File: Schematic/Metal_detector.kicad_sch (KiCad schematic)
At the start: 56 parts, among them J1 3.5mm jack, Q1 BC550, U1 NUCLEO64-F411RE, U2 LM393, U3 PCA9635

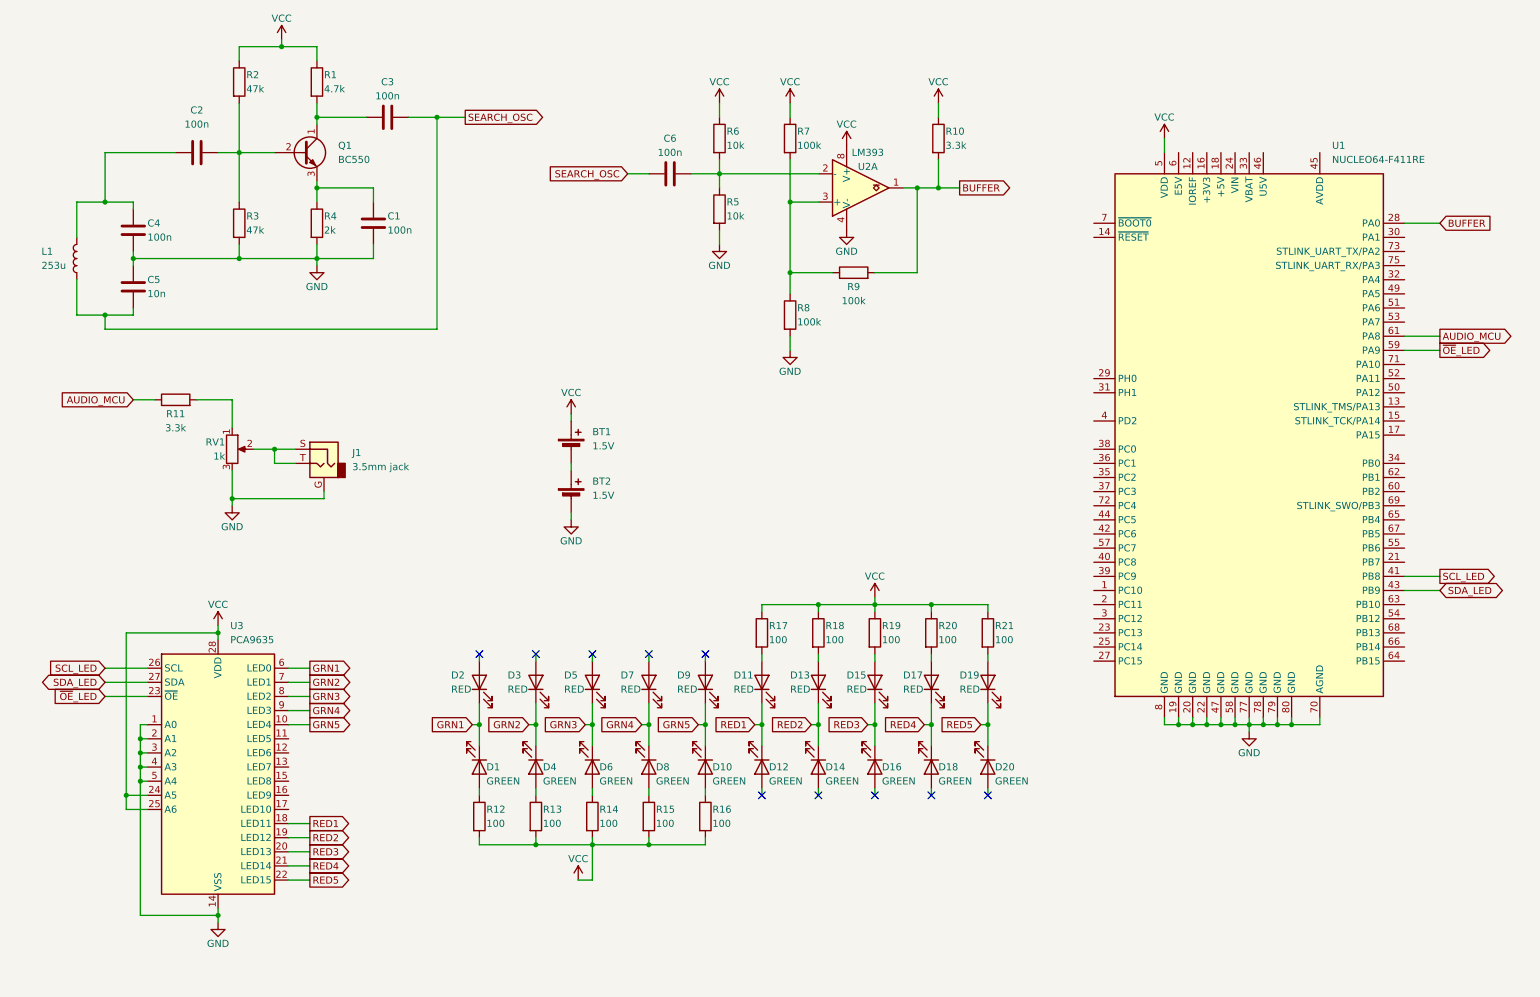
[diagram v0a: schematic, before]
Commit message: Added block diagram and schematic
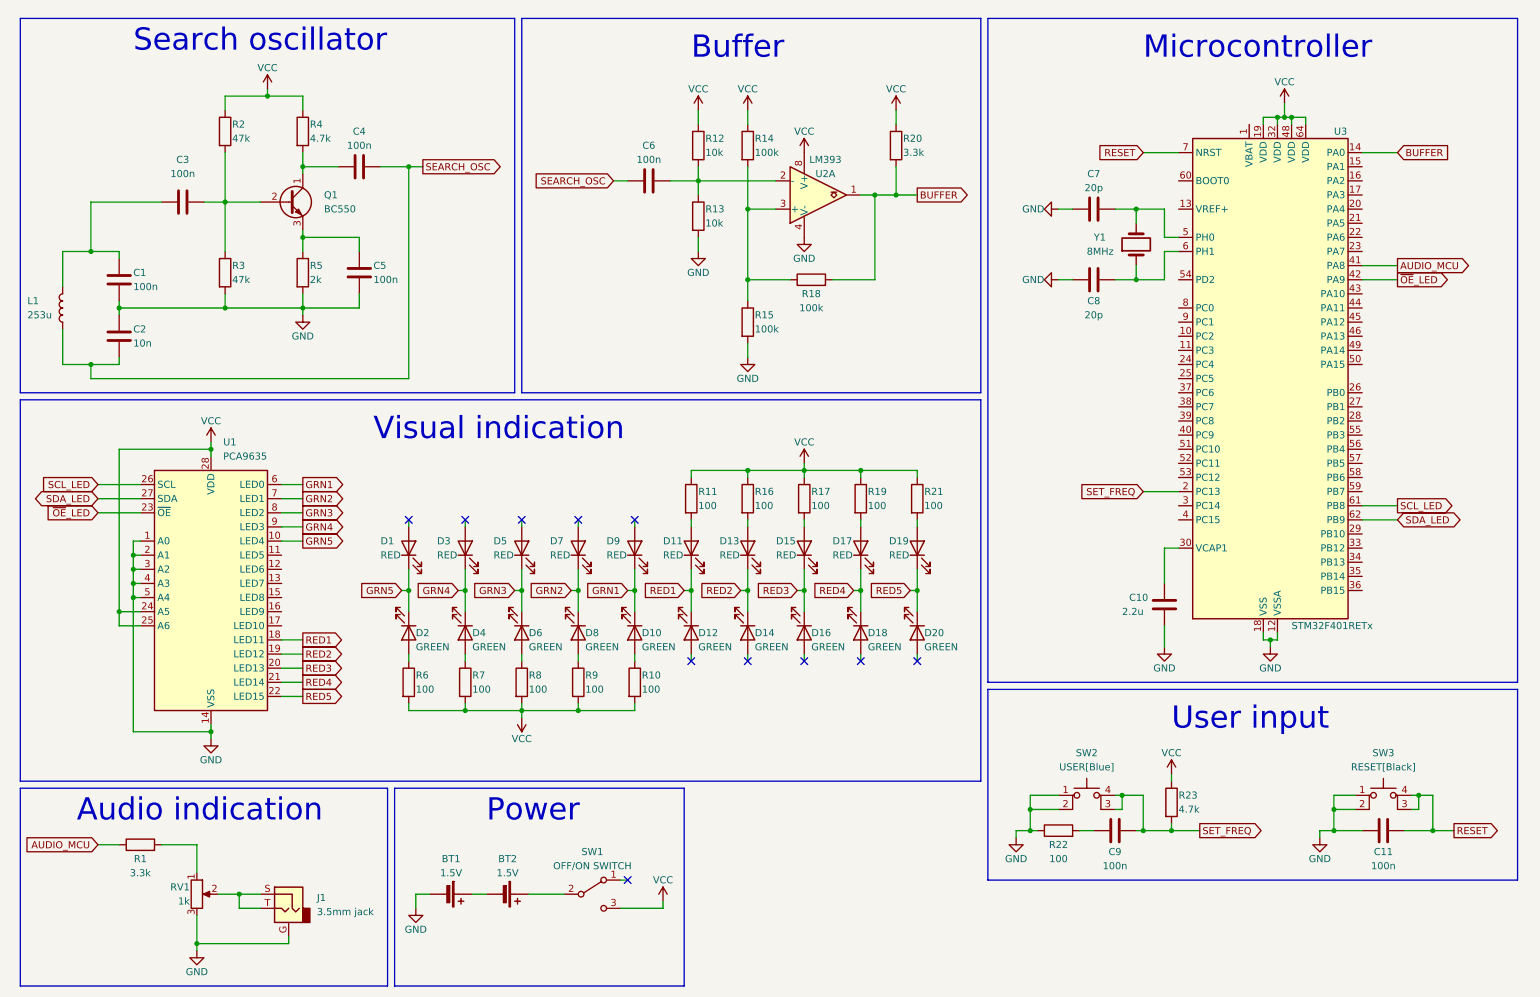
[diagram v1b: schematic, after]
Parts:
- removed U1: NUCLEO64-F411RE, Module:ST_Morpho_Connector_144_STLink, symbol MCU_Module:NUCLEO64-F411RE
- added C10: 2.2u, symbol Device:C
- added C11, C9: 100n, symbol Device:C
- added C7, C8: 20p, symbol Device:C
- added R22: 100, symbol Device:R
- added R23: 4.7k, symbol Device:R
- added SW1: OFF/ON SWITCH, symbol Switch:SW_SPDT
- added SW2: USER[Blue], symbol Switch:SW_MEC_5E
- added SW3: RESET[Black], symbol Switch:SW_MEC_5E
- added U3: STM32F401RETx, Package_QFP:LQFP-64_10x10mm_P0.5mm, symbol MCU_ST_STM32F4:STM32F401RETx
- added Y1: 8MHz, symbol Device:Crystal
- renumbered C4 to C1, C5 to C2, C2 to C3, C3 to C4, C1 to C5, D2 to D1, D1 to D2, R11 to R1, R16 to R10, R17 to R11, R6 to R12, R5 to R13, R7 to R14, R8 to R15, R18 to R16, R19 to R17, R9 to R18, R20 to R19, R10 to R20, R1 to R4, R4 to R5, R12 to R6, R13 to R7, R14 to R8, R15 to R9, U3 to U1
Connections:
- net AUDIO_MCU: now also U3.41 (PA8)
- net BUFFER: now also U3.14 (PA0)
- net GND: now also BT1.2 (-), C10.2, C11.1, C7.1, C8.1, R22.1, SW2.1, SW2.2, SW3.1, SW3.2, U3.12 (VSSA), U3.18 (VSS), U3.31 (VSS), U3.47 (VSS), U3.63 (VSS); no longer BT2.2 (-)
- net GRN1: now also D10.1 (K), D9.1 (K); no longer D1.1 (K), D2.1 (K)
- net GRN2: now also D7.1 (K), D8.1 (K); no longer D3.1 (K), D4.1 (K)
- net GRN4: now also D3.1 (K), D4.1 (K); no longer D7.1 (K), D8.1 (K)
- net GRN5: now also D1.1 (K), D2.1 (K); no longer D10.1 (K), D9.1 (K)
- net SCL_LED: now also U3.61 (PB8)
- net SDA_LED: now also U3.62 (PB9)
- net VCC: now also R23.1, SW1.3 (C), U3.19 (VDD), U3.32 (VDD), U3.48 (VDD), U3.64 (VDD); no longer BT1.1 (+)
- net ~{OE}_LED: now also U3.42 (PA9)
- net at BT2.1 (+): now also SW1.2 (B); no longer BT1.2 (-)
- new net: C10.1, U3.30 (VCAP1)
- new net: C9.1, R22.2
- new net: C7.2, U3.5 (PH0), Y1.2
- new net: C8.2, U3.6 (PH1), Y1.1
- new net: BT1.1 (+), BT2.2 (-)
- new net RESET: C11.2, SW3.3 (K), SW3.4 (A), U3.7 (NRST)
- new net SET_FREQ: C9.2, R23.2, SW2.3 (K), SW2.4 (A), U3.2 (PC13)
- no-connect marks 10 -> 11
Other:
- note added: "Audio indication"
- note added: "Buffer"
- note added: "Microcontroller"
- note added: "Power"
- note added: "Search oscillator"
- note added: "User input"
- note added: "Visual indication"
- company: (none) -> TU-Sofia
- title: (none) -> Metal detector
- moved on the sheet: C1, C2, C3, C4, C5, C6, D1, D10, D11, D12, D13, D14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

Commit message: Edited the oscillator block and wrote documentation for it
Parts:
- added C12: 47u, symbol Device:C_Polarized
- added C13, C14, C15, C16: 100n, symbol Device:C
- added R24: 1, symbol Device:R
- L1: value 253u -> 281u
- R14, R15: value 100k -> 10k
- R2: value 47k -> 20k
- R3: value 47k -> 10k
- R4: value 4.7k -> 1.2k
- R5: value 2k -> 330
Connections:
- net GND: now also C12.2, C13.2, C14.2, C15.2, C16.2
- net VCC: now also C13.1, C14.1, C15.1, C16.1, R24.1
- new net: C12.1, R24.2
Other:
- note added: "IC filter caps"
- note added: "Osc filter"

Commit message: Edited and documented the search oscillator, buffer and mcu blocks
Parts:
- removed C14: 100n, symbol Device:C
- added R24: 10k, symbol Device:R
- C14: renamed from C10; value 2.2u -> 4.7u
- C5: value 100n -> 1u
- renumbered C16 to C10, C7 to C11, C8 to C12, C9 to C13, C11 to C15, C12 to C7, C13 to C8, C15 to C9, R24 to R12, R12 to R13, R13 to R14, R14 to R15, R15 to R16, R16 to R17, R17 to R18, R18 to R19, R19 to R20, R20 to R21, R21 to R22, R22 to R23, R23 to R25
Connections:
- net GND: now also R24.1
- net VCC: now also U3.1 (VBAT)
- net at U3.60 (BOOT0): now also R24.2
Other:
- moved on the sheet: C11, C12, Y1

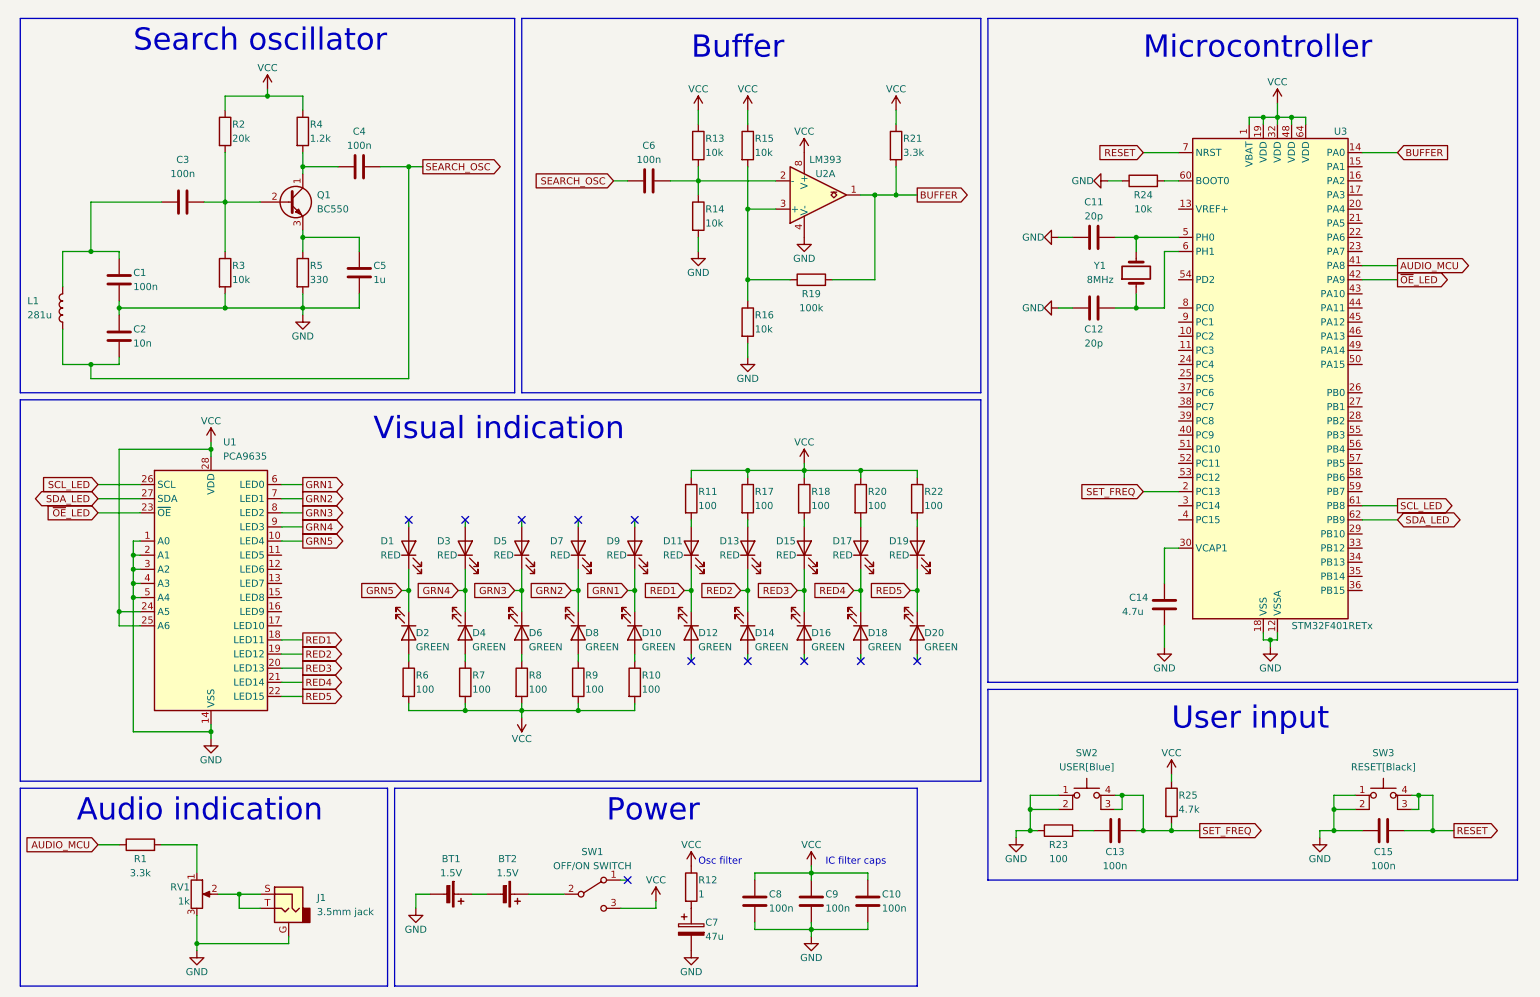
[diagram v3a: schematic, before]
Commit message: Documented all blocks, made some small changes to the schematic
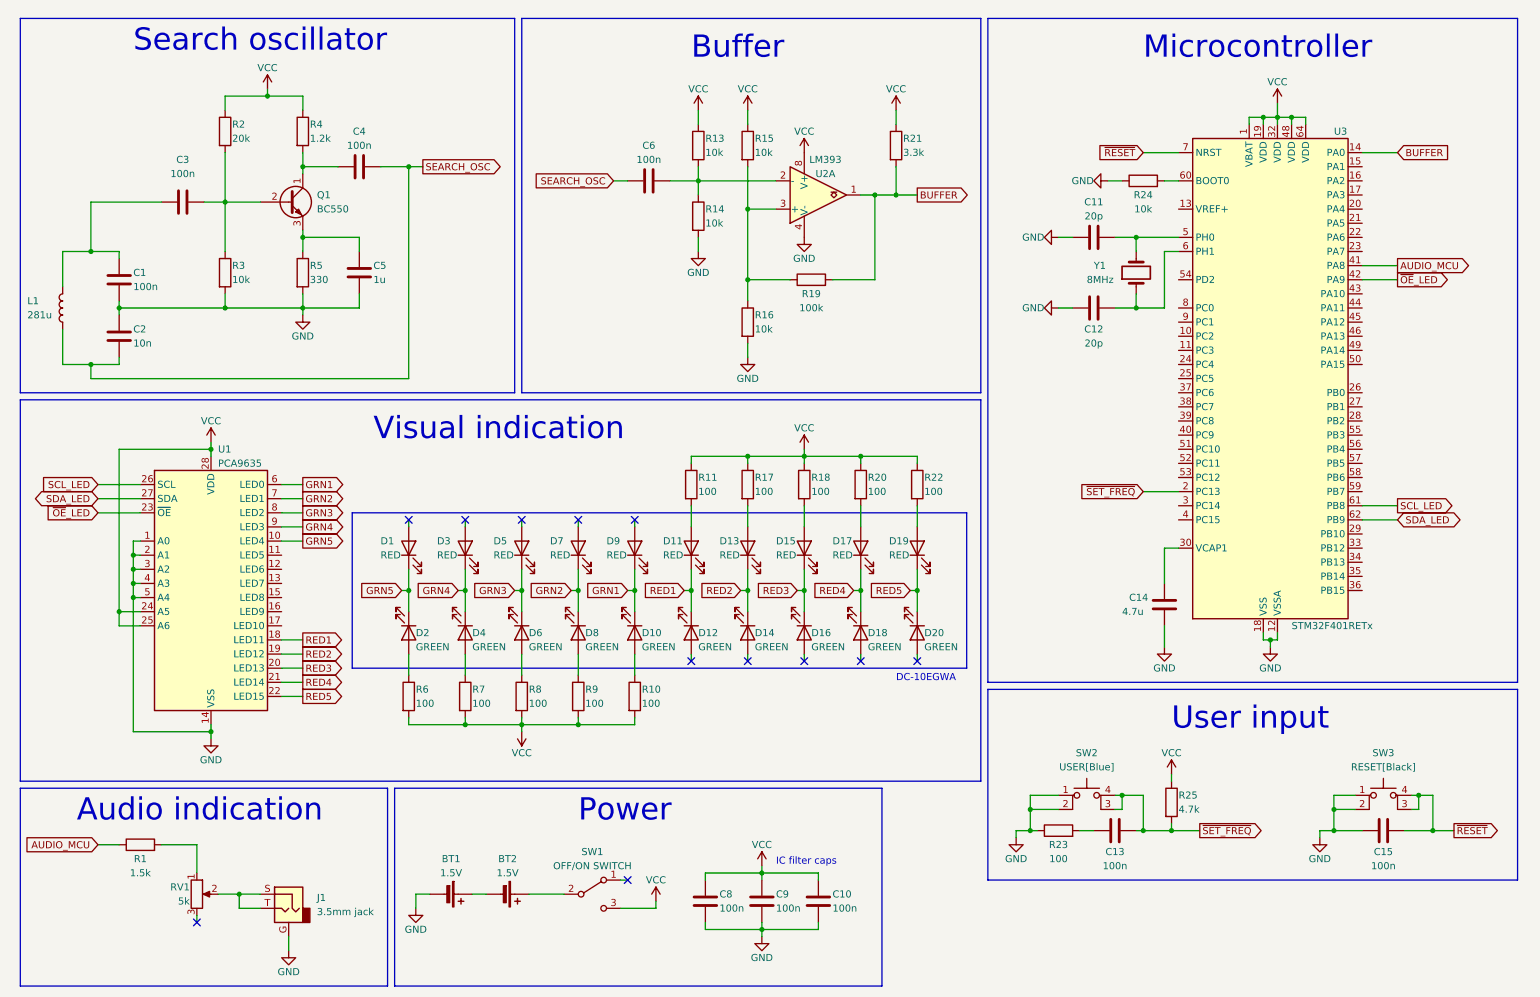
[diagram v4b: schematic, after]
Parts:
- removed C7: 47u, symbol Device:C_Polarized
- removed R12: 1, symbol Device:R
- R1: value 3.3k -> 1.5k
- RV1: value 1k -> 5k
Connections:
- net GND: no longer RV1.3
- net RESET renamed ~{RESET}
- net SET_FREQ renamed ~{SET_FREQ}
- no-connect marks 11 -> 12
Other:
- note added: "DC-10EGWA"
- note removed: "Osc filter"
- moved on the sheet: C10, C8, C9, R10, R11, R17, R18, R20, R22, R6, R7, R8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
